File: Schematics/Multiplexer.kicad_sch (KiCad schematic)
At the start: 87 parts, among them J5 Conn_01x04, J6 Conn_01x03, J7 Conn_01x04, J76 Conn_01x04, J77 Conn_01x04, J78 Conn_01x04, J79 Conn_01x04, J8 Conn_01x02, J80 Conn_01x04, J9 Conn_01x03, J90 Conn_01x04, Q11 BSS138, Q12 BSS138, U10 TL072, U103 DG212C, U106 DG212C, U5 DG212C, U6 DG212C, U72 LM1117-3.3, U8 PCF8575, U9 LM1117-5

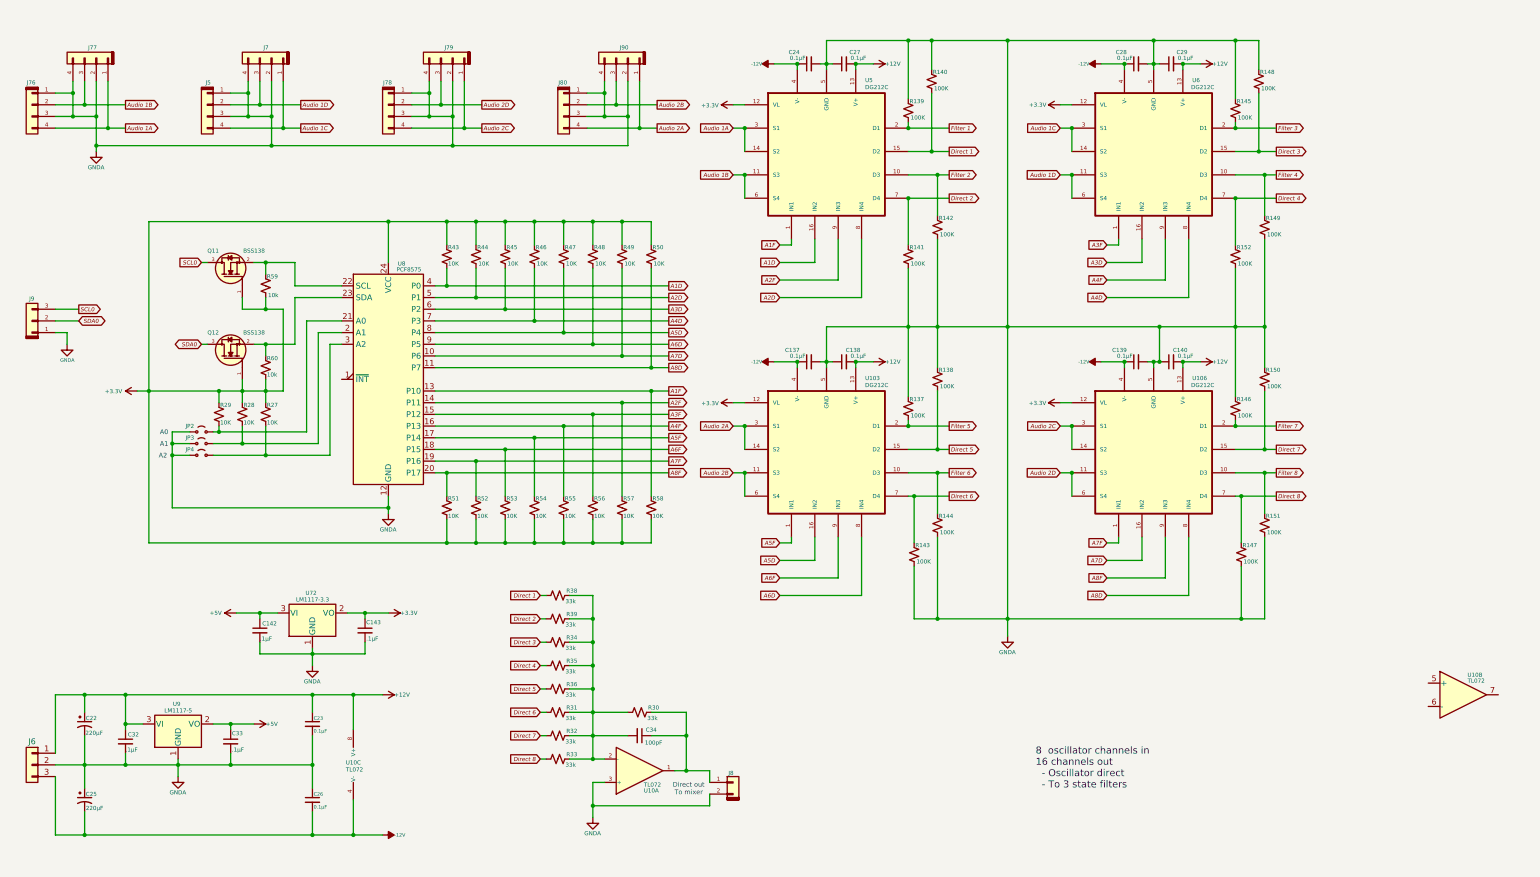
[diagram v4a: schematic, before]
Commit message: Upgreade byte value interface to short.  First stage of refactoring midi input for rotory encoders.  Still needs scaling.
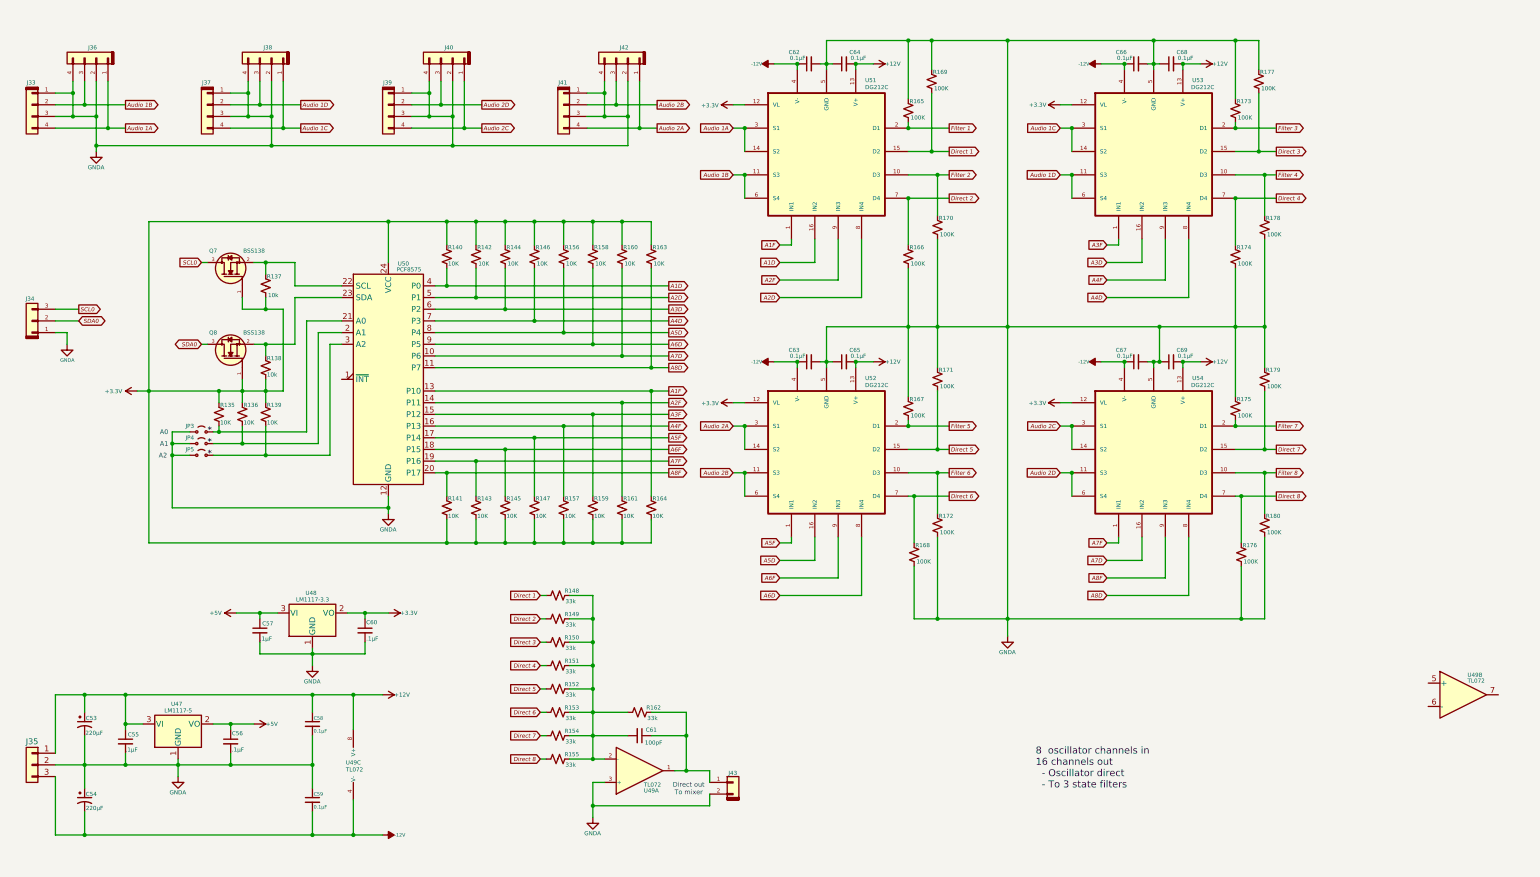
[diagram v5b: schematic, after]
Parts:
- renumbered C22 to C53, C25 to C54, C32 to C55, C33 to C56, C142 to C57, C23 to C58, C26 to C59, C143 to C60, C34 to C61, C24 to C62, C137 to C63, C27 to C64, C138 to C65, C28 to C66, C139 to C67, C29 to C68, C140 to C69, J76 to J33, J9 to J34, J6 to J35, J77 to J36, J5 to J37, J7 to J38, J78 to J39, J79 to J40, J80 to J41, J90 to J42, J8 to J43, JP2 to JP3, JP3 to JP4, JP4 to JP5, Q11 to Q7, Q12 to Q8, R29 to R135, R28 to R136, R59 to R137, R60 to R138, R27 to R139, R43 to R140, R51 to R141, R44 to R142, R52 to R143, R45 to R144, R53 to R145, R46 to R146, R54 to R147, R38 to R148, R39 to R149, R34 to R150, R35 to R151, R36 to R152, R31 to R153, R32 to R154, R33 to R155, R47 to R156, R55 to R157, R48 to R158, R56 to R159, R49 to R160, R57 to R161, R30 to R162, R50 to R163, R58 to R164, R139 to R165, R141 to R166, R137 to R167, R143 to R168, R140 to R169, R142 to R170, R138 to R171, R144 to R172, R145 to R173, R152 to R174, R146 to R175, R147 to R176, R148 to R177, R149 to R178, R150 to R179, R151 to R180, U9 to U47, U72 to U48, U10 to U49, U8 to U50, U5 to U51, U103 to U52, U6 to U53, U106 to U54
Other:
- note added: "*"

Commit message: Updated schematics including VCO and VCF daughter boards
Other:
- title: (none) -> Signal Multiplexer
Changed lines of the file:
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@@
 	(generator_version "8.0")
 	(paper "USLegal")
+	(title_block
+		(title "Signal Multiplexer")
+		(date "2025-01-16")
+		(rev "1.2")
+		(comment 1 "In Development ")
+	)
 	(junction
 		(at 39.37 179.07)
@@
 	(text "8  oscillator channels in\n16 channels out\n  - Oscillator direct\n  - To 3 state filters"
 		(exclude_from_sim no)
-		(at 237.236 179.832 0)
+		(at 308.61 180.34 0)
 		(effects
 			(font

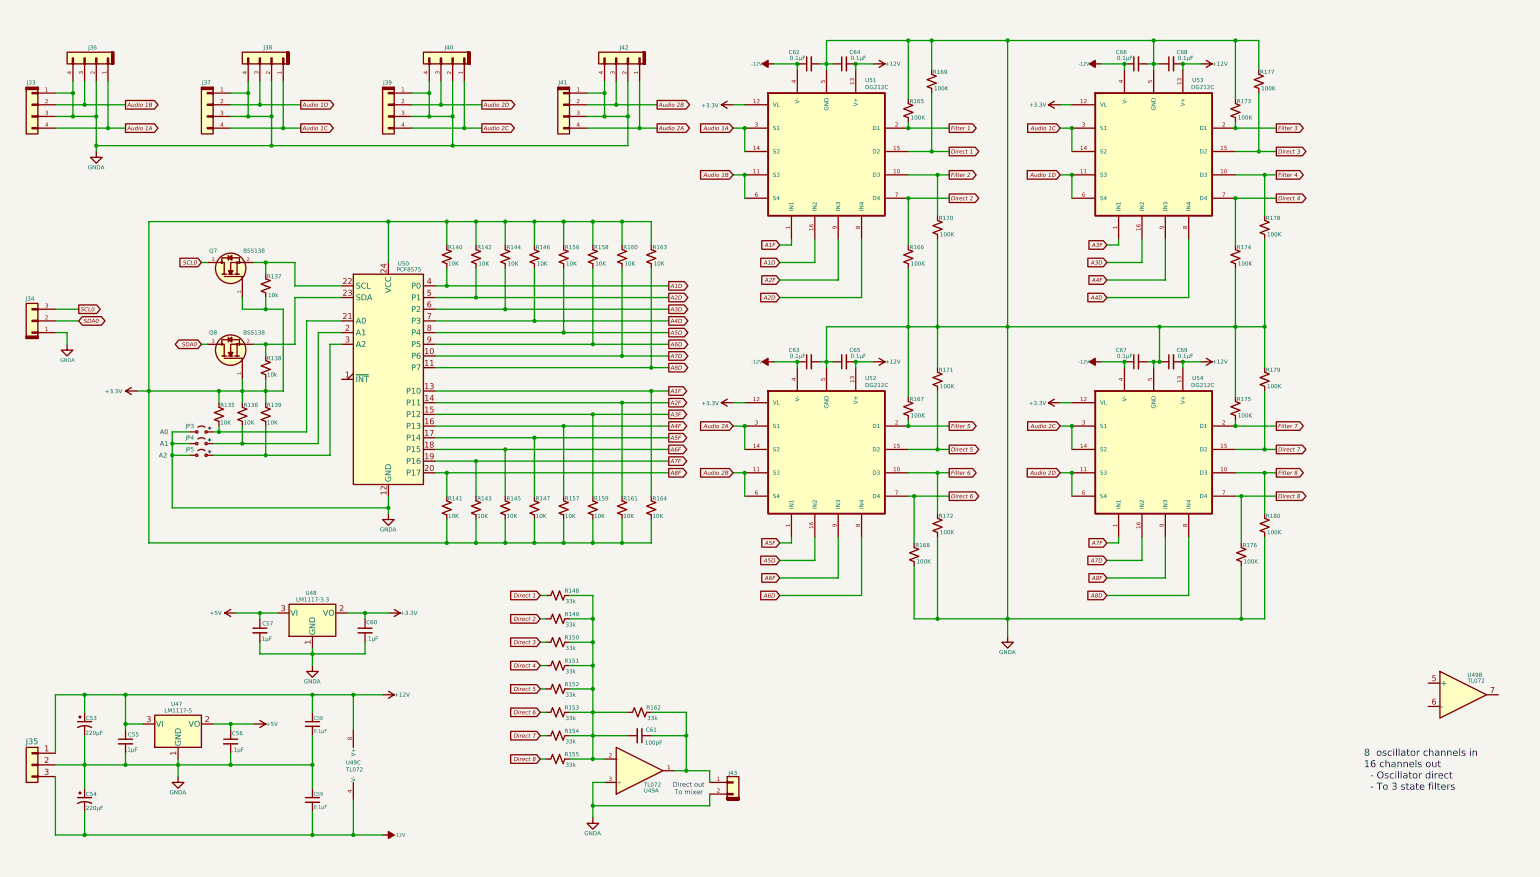
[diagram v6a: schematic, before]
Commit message: Cleaned up page advance on display controls.
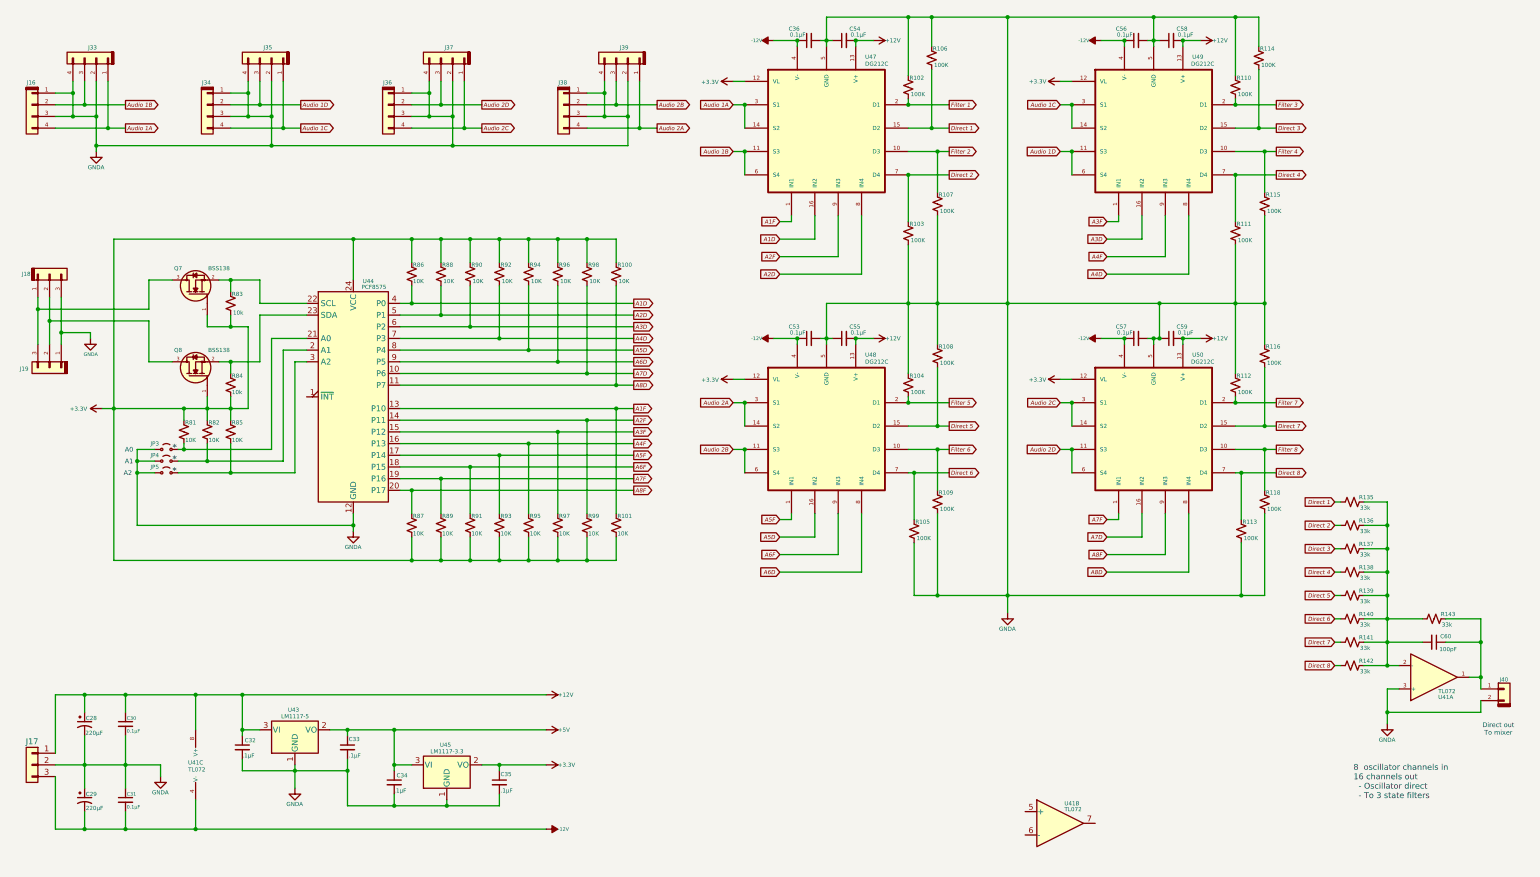
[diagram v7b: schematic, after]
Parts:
- removed J34: Conn_01x03, symbol My Connectors:Conn_01x03
- added J18, J19: Conn_01x03, symbol My Connectors:Conn_01x03
- renumbered C53 to C28, C54 to C29, C58 to C30, C59 to C31, C55 to C32, C56 to C33, C57 to C34, C60 to C35, C62 to C36, C63 to C53, C64 to C54, C65 to C55, C66 to C56, C67 to C57, C68 to C58, C69 to C59, C61 to C60, J33 to J16, J35 to J17, J36 to J33, J37 to J34, J38 to J35, J39 to J36, J40 to J37, J41 to J38, J42 to J39, J43 to J40, R163 to R100, R164 to R101, R165 to R102, R166 to R103, R167 to R104, R168 to R105, R169 to R106, R170 to R107, R171 to R108, R172 to R109, R173 to R110, R174 to R111, R175 to R112, R176 to R113, R177 to R114, R178 to R115, R179 to R116, R180 to R118, R148 to R135, R149 to R136, R150 to R137, R151 to R138, R152 to R139, R153 to R140, R154 to R141, R155 to R142, R162 to R143, R135 to R81, R136 to R82, R137 to R83, R138 to R84, R139 to R85, R140 to R86, R141 to R87, R142 to R88, R143 to R89, R144 to R90, R145 to R91, R146 to R92, R147 to R93, R156 to R94, R157 to R95, R158 to R96, R159 to R97, R160 to R98, R161 to R99, U49 to U41, U47 to U43, U50 to U44, U48 to U45, U51 to U47, U52 to U48, U53 to U49, U54 to U50
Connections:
- net GNDA: now also J18.3 (Pin_3), J19.1 (Pin_1)
- net SCL0: no longer names the net of Q7.3
- net SCL0: now also J18.1 (Pin_1), J19.3 (Pin_3)
- net SDA0: no longer names the net of Q8.3
- net SDA0: now also J18.2 (Pin_2), J19.2 (Pin_2)
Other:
- moved on the sheet: C30, C31, C32, C33, C34, C35, C36, C53, C54, C55, C56, C57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

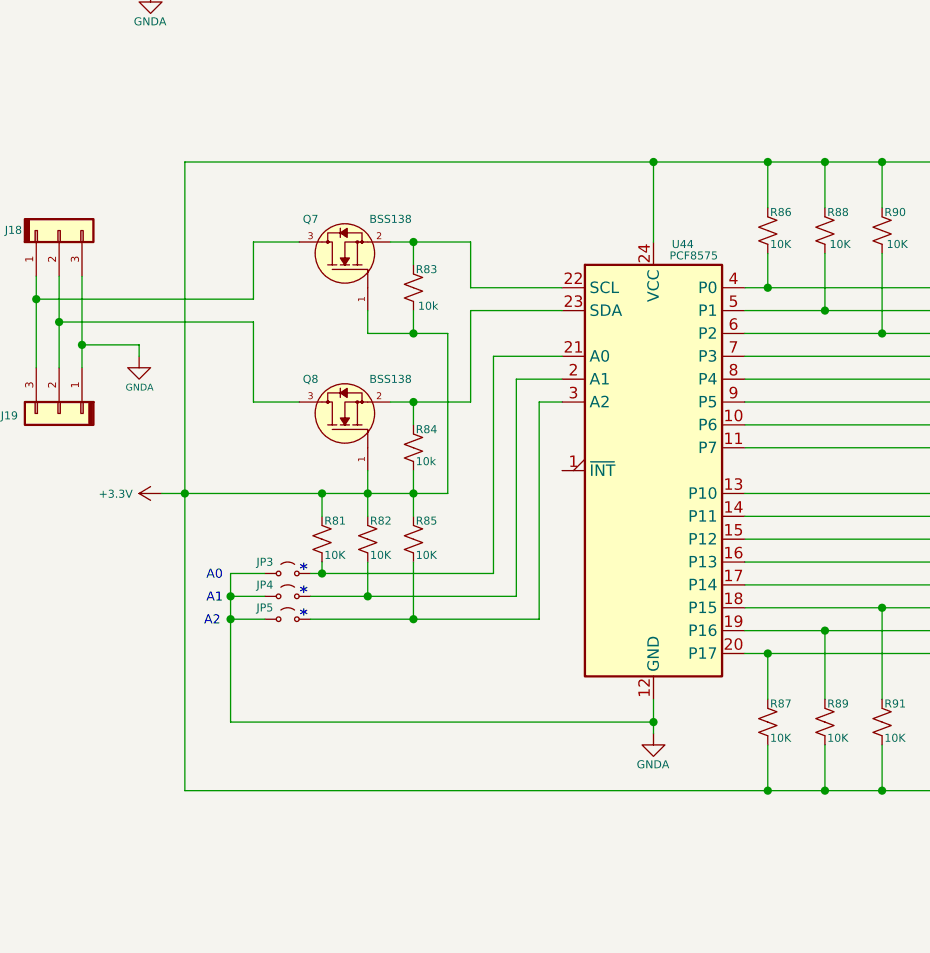
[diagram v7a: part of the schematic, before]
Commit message: minor adjustments for modulation control interface.
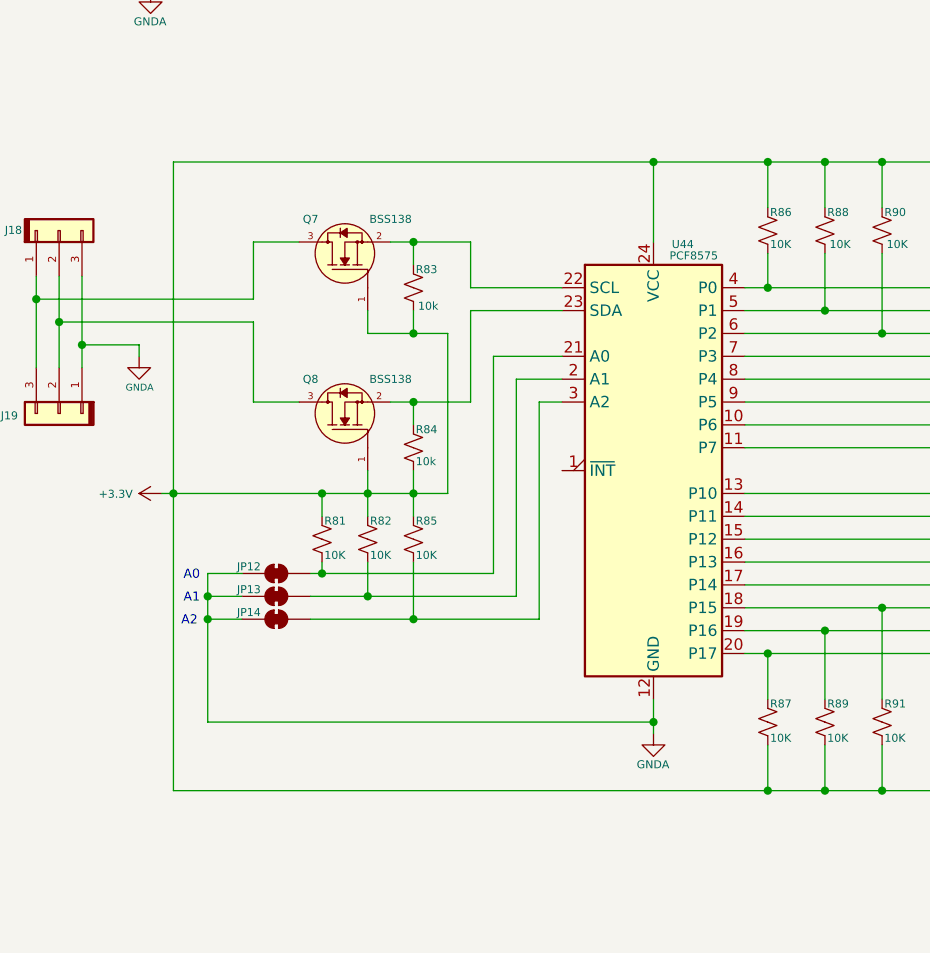
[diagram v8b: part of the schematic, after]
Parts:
- removed JP3, JP4, JP5: Jumper_2_Small_Open, symbol Jumper:Jumper_2_Small_Open
- added JP12, JP13, JP14: ~, symbol Jumper:SolderJumper_2_Bridged
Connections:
- net GNDA: now also JP12.1 (A), JP13.1 (A), JP14.1 (A)
- net at R85.2, U44.3 (A2): now also JP14.2 (B)
- net at R82.2, U44.2 (A1): now also JP13.2 (B)
- net at R81.2, U44.21 (A0): now also JP12.2 (B)
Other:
- note removed: "*"
